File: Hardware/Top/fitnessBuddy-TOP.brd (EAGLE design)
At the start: 38 x 38 mm, 51 parts, among them SW1 SWITCH.MOM, SW2 SWITCH.MOM, U2 NRF52832_MODULE_MDBT42, U4 PCF8523

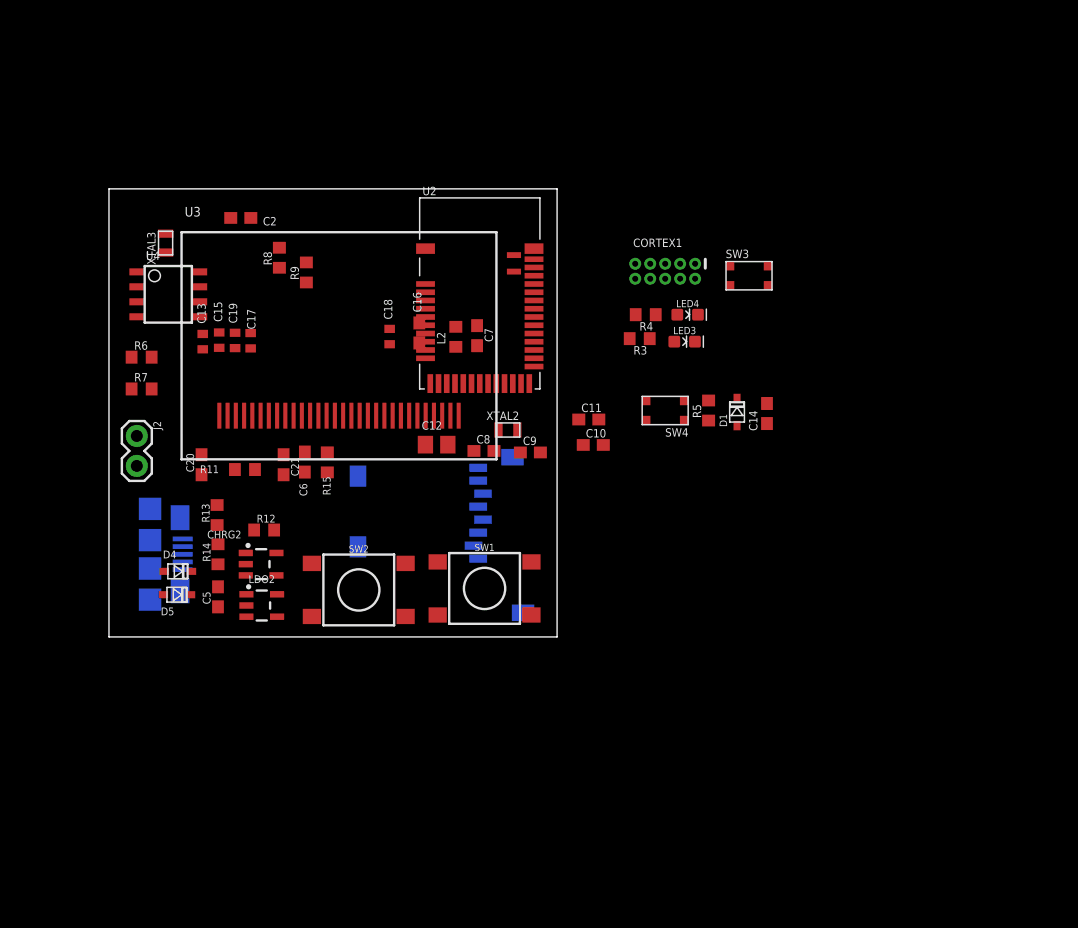
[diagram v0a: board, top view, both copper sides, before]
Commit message: added FTDI controller
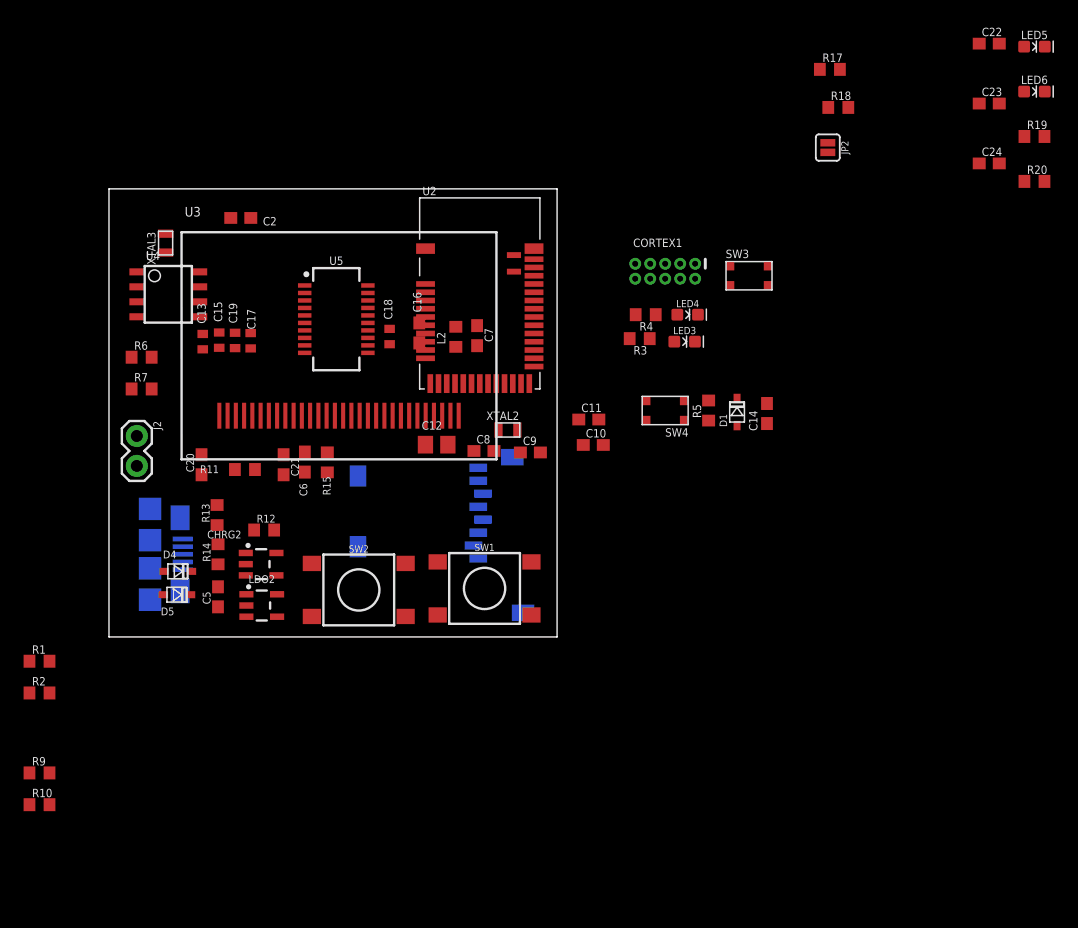
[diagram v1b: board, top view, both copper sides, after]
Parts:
- removed R8: 10k, LinnesLab-Passives:R0603
- added C22: 100n, LinnesLab-Passives:C0603
- added C23, C24: 47p, LinnesLab-Passives:C0603
- added JP2: (no value), LinnesLab-Switches:SMT-JUMPER_2_NO_SILK
- added LED5: RED, LinnesLab-LED:LED-0603
- added LED6: YELLOW, LinnesLab-LED:LED-0603
- added R1, R2: 0, LinnesLab-Passives:R0603
- added R10: 10k, LinnesLab-Passives:R0603
- added R17, R18: 27, LinnesLab-Passives:R0603
- added R19, R20: 1k, LinnesLab-Passives:R0603
- added U5: FT231XS, LinnesLab-DigitalIC:SSOP20_L
- moved R9 48.1 mm to (-5.89, -11.5), turned to 0 degrees
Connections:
- removed net RXD: U2.21
- removed net TXD: U2.19
- new net !CTS: JP2.2, U5.9
- new net !DTR: U5.1
- new net FT3V3: U5.13
- new net N$23: R17.2, U5.12
- new net N$24: R18.2, U5.11
- new net N$25: LED5.C, R19.2
- new net N$26: LED6.C, R20.2
- new net RXD.FT: R2.1, U5.4
- new net RXD.NRF: R1.2, U2.21
- new net RXLED: R19.1, U5.17
- new net TXD.FT: R1.1, U5.20
- new net TXD.NRF: R2.2, U2.19
- new net TXLED: R20.1, U5.10
- net 3.3V: now also C22.2, LED5.A, LED6.A, R10.2, U5.14, U5.3; no longer R8.2
- net GND: now also C22.1, C23.2, C24.1, JP2.1, U5.16, U5.6
- net SCL: now also R10.1; no longer R8.1
- net USB+: now also C23.1, R18.1
- net USB-: now also C24.2, R17.1
- net V_USB: now also U5.15

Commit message: finished bottom board and schematic
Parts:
- moved XTAL3 2.93 mm to (1.88, 33.2)
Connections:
- removed net BATT: R13.1, R14.2
- removed net CD1: SD2.CD1
- removed net CHRG.STAT: CHRG2.1, R12.1
- removed net CS.OLED: U3.13
- removed net DC.OLED: U3.15
- removed net RESET.OLED: U3.14
- removed net SD.CS: SD2.2
- removed net SW1: SW1.A1, SW2.A1
- new net A4/BATT: R13.1, R14.2, U2.5
- new net A6/TIA: U2.7
- new net A7/PPG: U2.8
- new net D11/SW1: SW1.A1, U2.25
- new net D15/SW2: SW2.A1, U2.29
- new net D16/CS.OLED: U2.30, U3.13
- new net D27/CHRG.STATUS: CHRG2.1, R12.1, U2.4
- new net D29/LED.CTRL: U2.6
- new net D3/RESET.OLED: U2.16, U3.14
- new net D4/DC.OLED: U2.17, U3.15
- new net D5/CD1: SD2.CD1, U2.18
- new net D7/SD.CS: SD2.2, U2.20
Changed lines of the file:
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@@
 <attribute name="VALUE" x="11.811" y="37.4396" size="0.7112" layer="27" rot="R180"/>
 </element>
-<element name="XTAL3" library="LinnesLab-Clocks" package="2-SMD.NOLEAD.2.0MMTO1.2MM" package3d_urn="urn:adsk.eagle:package:18579459/2" value="32.7680kHz" x="4.8006" y="33.401" smashed="yes" rot="R90">
-<attribute name="NAME" x="3.949" y="31.5686" size="0.7112" layer="25" rot="R90"/>
-<attribute name="VALUE" x="6.4958" y="31.6702" size="0.7112" layer="27" rot="R90"/>
+<element name="XTAL3" library="LinnesLab-Clocks" package="2-SMD.NOLEAD.2.0MMTO1.2MM" package3d_urn="urn:adsk.eagle:package:18579459/2" value="32.7680kHz" x="1.8796" y="33.1724" smashed="yes" rot="R90">
+<attribute name="NAME" x="1.028" y="31.34" size="0.7112" layer="25" rot="R90"/>
+<attribute name="VALUE" x="3.5748" y="31.4416" size="0.7112" layer="27" rot="R90"/>
 </element>
 <element name="U4" library="LinnesLab-Clocks" package="SO8" package3d_urn="urn:adsk.eagle:package:18599600/2" value="PCF8523" x="5.0292" y="29.0576" smashed="yes">
@@
 <contactref element="U2" pad="38"/>
 </signal>
-<signal name="DC.OLED">
-<contactref element="U3" pad="15"/>
-</signal>
-<signal name="RESET.OLED">
-<contactref element="U3" pad="14"/>
-</signal>
 <signal name="N$1">
 <contactref element="U3" pad="11"/>
@@
 <wire x1="27.5572" y1="18.7644" x2="23.7998" y2="26.1262" width="0" layer="19" extent="1-1"/>
 </signal>
-<signal name="CS.OLED">
-<contactref element="U3" pad="13"/>
-</signal>
 <signal name="CD2">
 <contactref element="SD2" pad="CD2"/>
-</signal>
-<signal name="CD1">
-<contactref element="SD2" pad="CD1"/>
-</signal>
-<signal name="SD.CS">
-<contactref element="SD2" pad="2"/>
 </signal>
 <signal name="N$17">
@@
 <wire x1="4.6158" y1="3.5814" x2="6.2548" y2="5.7104" width="0" layer="19" extent="1-16"/>
 </signal>
-<signal name="CHRG.STAT">
-<contactref element="R12" pad="1"/>
-<contactref element="CHRG2" pad="1"/>
-<wire x1="12.3072" y1="9.0678" x2="11.6031" y2="7.1222" width="0" layer="19" extent="1-1"/>
-</signal>
 <signal name="USB-">
 <contactref element="USB2" pad="2"/>
@@
 <wire x1="60.999" y1="44.9072" x2="73.8006" y2="45.2374" width="0" layer="19" extent="1-1"/>
 <wire x1="6.2548" y1="7.0104" x2="60.999" y2="44.9072" width="0" layer="19" extent="1-16"/>
-</signal>
-<signal name="BATT">
-<contactref element="R13" pad="1"/>
-<contactref element="R14" pad="2"/>
-<wire x1="9.2456" y1="7.8604" x2="9.1694" y2="9.4878" width="0" layer="19" extent="1-1"/>
 </signal>
 <signal name="VIN">
@@
 <contactref element="XTAL3" pad="P$1"/>
 <contactref element="U4" pad="2"/>
-<wire x1="4.8006" y1="32.601" x2="2.3792" y2="29.6926" width="0" layer="19" extent="1-1"/>
+<wire x1="1.8796" y1="32.3724" x2="2.3792" y2="29.6926" width="0" layer="19" extent="1-1"/>
 </signal>
 <signal name="N$20">
 <contactref element="XTAL3" pad="P$2"/>
 <contactref element="U4" pad="1"/>
-<wire x1="4.8006" y1="34.201" x2="2.3792" y2="30.9626" width="0" layer="19" extent="1-1"/>
+<wire x1="1.8796" y1="33.9724" x2="2.3792" y2="30.9626" width="0" layer="19" extent="1-1"/>
 </signal>
 <signal name="VBATT">
 <contactref element="U4" pad="3"/>
-</signal>
-<signal name="SW1">
-<contactref element="SW1" pad="A1"/>
-<contactref element="SW2" pad="A1"/>
-<wire x1="27.8766" y1="1.8648" x2="17.2086" y2="1.7378" width="0" layer="19" extent="1-1"/>
 </signal>
 <signal name="N$23">
@@
 <wire x1="-5.0428" y1="-4.7498" x2="32.1452" y2="21.4838" width="0" layer="19" extent="1-1"/>
 </signal>
+<signal name="D27/CHRG.STATUS">
+<contactref element="U2" pad="4"/>
+<contactref element="R12" pad="1"/>
+<contactref element="CHRG2" pad="1"/>
+<wire x1="12.3072" y1="9.0678" x2="26.8452" y2="28.5338" width="0" layer="19" extent="1-1"/>
+<wire x1="11.6031" y1="7.1222" x2="12.3072" y2="9.0678" width="0" layer="19" extent="1-1"/>
+</signal>
+<signal name="A4/BATT">
+<contactref element="U2" pad="5"/>
+<contactref element="R13" pad="1"/>
+<contactref element="R14" pad="2"/>
+<wire x1="9.1694" y1="9.4878" x2="26.8452" y2="27.8338" width="0" layer="19" extent="1-1"/>
+<wire x1="9.2456" y1="7.8604" x2="9.1694" y2="9.4878" width="0" layer="19" extent="1-1"/>
+</signal>
+<signal name="D7/SD.CS">
+<contactref element="U2" pad="20"/>
+<contactref element="SD2" pad="2"/>
+<wire x1="30.9156" y1="7.7464" x2="32.8452" y2="21.4838" width="0" layer="19" extent="1-16"/>
+</signal>
+<signal name="D5/CD1">
+<contactref element="U2" pad="18"/>
+<contactref element="SD2" pad="CD1"/>
+<wire x1="21.1156" y1="13.6464" x2="31.4452" y2="21.4838" width="0" layer="19" extent="1-16"/>
+</signal>
+<signal name="D11/SW1">
+<contactref element="U2" pad="25"/>
+<contactref element="SW1" pad="A1"/>
+<wire x1="27.8766" y1="1.8648" x2="36.0452" y2="22.9338" width="0" layer="19" extent="1-1"/>
+</signal>
+<signal name="D15/SW2">
+<contactref element="U2" pad="29"/>
+<contactref element="SW2" pad="A1"/>
+<wire x1="17.2086" y1="1.7378" x2="36.0452" y2="25.7338" width="0" layer="19" extent="1-1"/>
+</signal>
+<signal name="D16/CS.OLED">
+<contactref element="U2" pad="30"/>
+<contactref element="U3" pad="13"/>
+<wire x1="17.7572" y1="18.7644" x2="36.0452" y2="26.4338" width="0" layer="19" extent="1-1"/>
+</signal>
+<signal name="D3/RESET.OLED">
+<contactref element="U2" pad="16"/>
+<contactref element="U3" pad="14"/>
+<wire x1="18.4572" y1="18.7644" x2="30.0452" y2="21.4838" width="0" layer="19" extent="1-1"/>
+</signal>
+<signal name="D4/DC.OLED">
+<contactref element="U2" pad="17"/>
+<contactref element="U3" pad="15"/>
+<wire x1="19.1572" y1="18.7644" x2="30.7452" y2="21.4838" width="0" layer="19" extent="1-1"/>
+</signal>
+<signal name="D29/LED.CTRL">
+<contactref element="U2" pad="6"/>
+</signal>
+<signal name="A6/TIA">
+<contactref element="U2" pad="7"/>
+</signal>
+<signal name="A7/PPG">
+<contactref element="U2" pad="8"/>
+</signal>
 </signals>

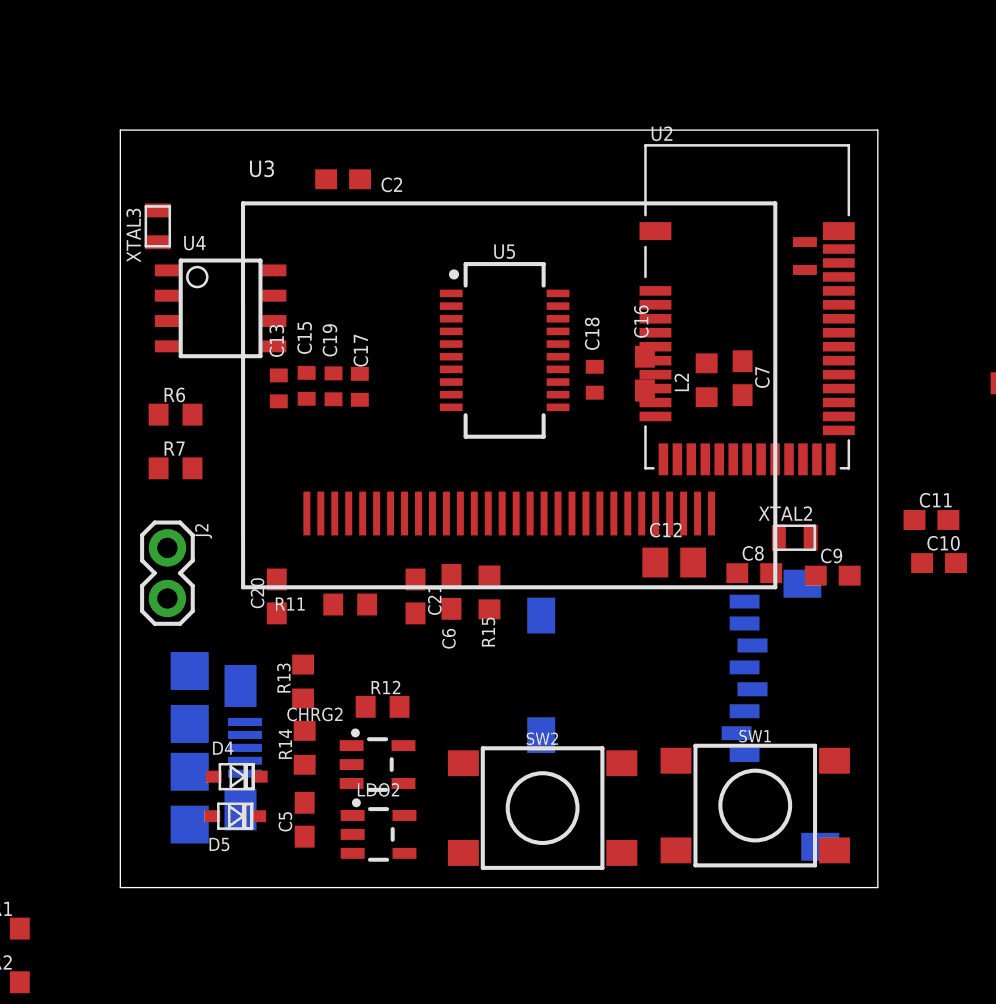
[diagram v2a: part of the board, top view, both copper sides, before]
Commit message: Made progress on routing bottom board
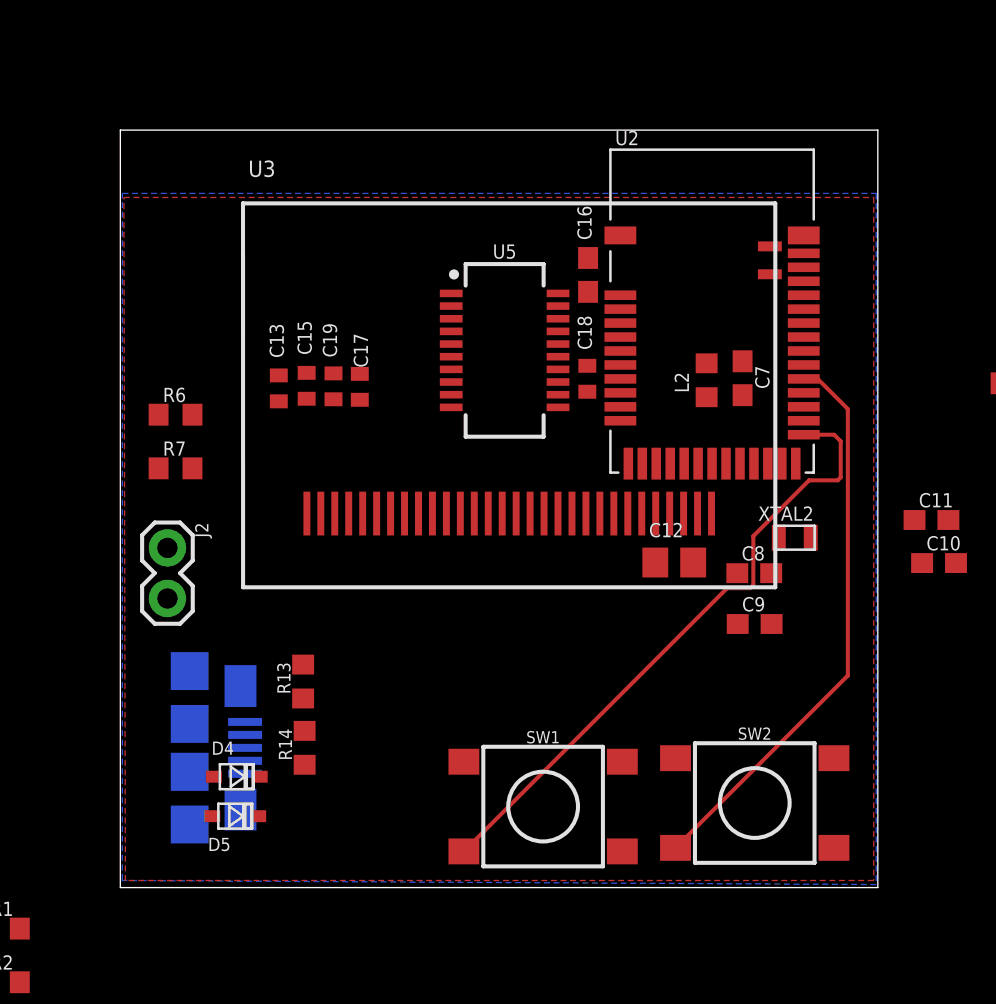
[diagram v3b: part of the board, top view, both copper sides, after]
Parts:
- removed C2, C5, C6: 1u, LinnesLab-Passives:C0603
- removed C20, C21: 4.7u, LinnesLab-Passives:C0603
- removed CHRG2: MCP73831, LinnesLab-Power:SOT23-5
- removed LDO2: MIC5504, LinnesLab-Power:SOT23-5
- removed R11: (no value), LinnesLab-Passives:R0603
- removed R12, R15: 100k, LinnesLab-Passives:R0603
- removed SD2: (no value), LinnesLab-Connectors:MICROSD
- removed U4: PCF8523, LinnesLab-Clocks:SO8
- removed XTAL3: 32.7680kHz, LinnesLab-Clocks:2-SMD.NOLEAD.2.0MMTO1.2MM
- moved SW2 10.6 mm to (31.8, 4.24)
- moved SW1 10.6 mm to (21.2, 4.06)
- moved C16 5.71 mm to (23.5, 30.7)
- moved C9 4.61 mm to (31.8, 13.2)
- moved U2 1.77 mm to (29.7, 28.9)
- moved C18 0.38 mm to (23.4, 25.5)
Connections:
- removed net CD2: SD2.CD2
- removed net N$17: CHRG2.5, R11.2
- removed net N$19: U4.2, XTAL3.P$1
- removed net N$20: U4.1, XTAL3.P$2
- removed net VBATT: U4.3
- net 3.3V: no longer C2.1, C6.1, LDO2.5, R15.2, SD2.4, U4.8
- net D27/CHRG.STATUS: no longer CHRG2.1, R12.1
- net D5/CD1: no longer SD2.CD1
- net D7/SD.CS: no longer SD2.2
- net GND: no longer C2.2, C20.2, C21.1, C5.1, C6.2, CHRG2.2, LDO2.2, R11.1, R15.1, SD2.6, SD2.MT1, SD2.MT2, U4.4
- net MISO: no longer SD2.7
- net MOSI: no longer SD2.3
- net SCK: no longer SD2.5
- net SCL: no longer U4.6
- net SDA: no longer U4.5
- net VIN: no longer C21.2, C5.2, CHRG2.4, LDO2.1, LDO2.3, R12.2
- net VLIPO: no longer C20.1, CHRG2.3
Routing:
- net D11/SW1: track 0.00 -> 31.9 mm
- net D15/SW2: track 0.00 -> 28.5 mm
- added copper zone on layer 1, net 3.3V
- added copper zone on layer 16, net GND
